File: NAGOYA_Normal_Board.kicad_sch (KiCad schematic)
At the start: 74 parts, among them CN1 value, CN10 value, CN11 value, CN12 value, CN13 value, CN14 RefereeSystem, CN2 value, CN3 value, CN4 value, CN5 value, CN6 value, CN7 value, CN8 value, CN9 value, J1 debug, Q2 DDTC114EUA-7-F, U1 Teensy4.1, U2 TCAN1042HVDR, U3 TCAN1042HVDR, U4 TCAN1042HVDR, U6 TLP172AM, U7 BNO055, Y2 32.768 k

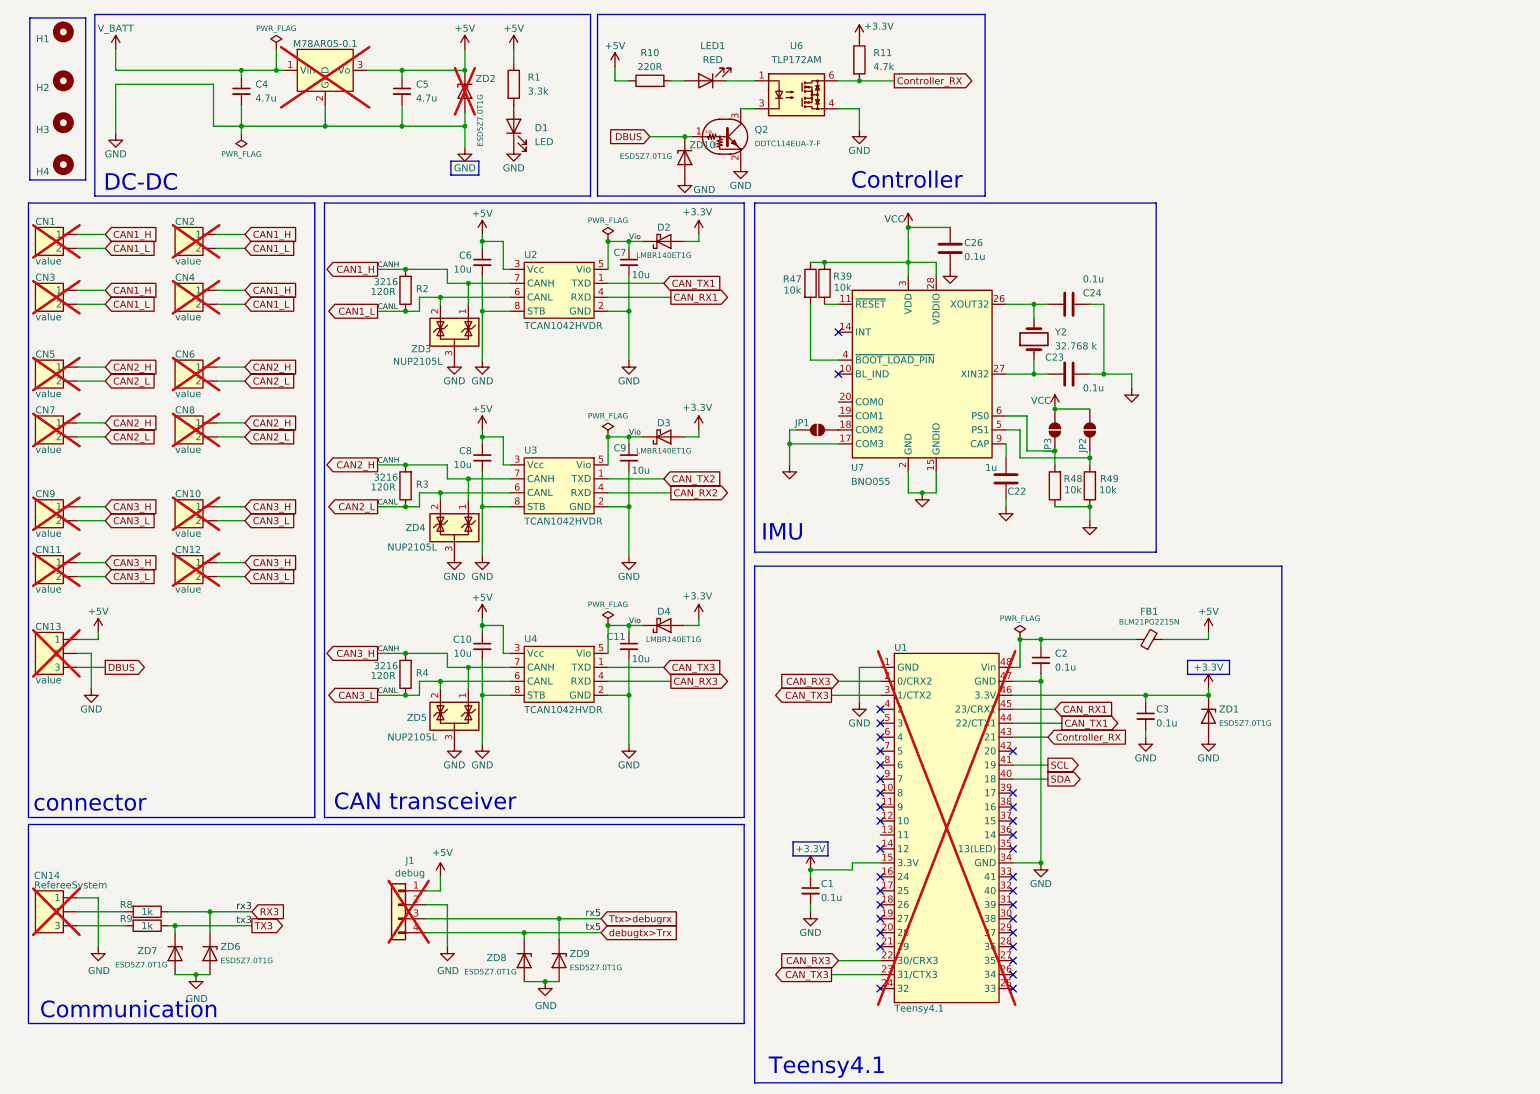
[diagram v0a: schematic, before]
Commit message: RS485を追加
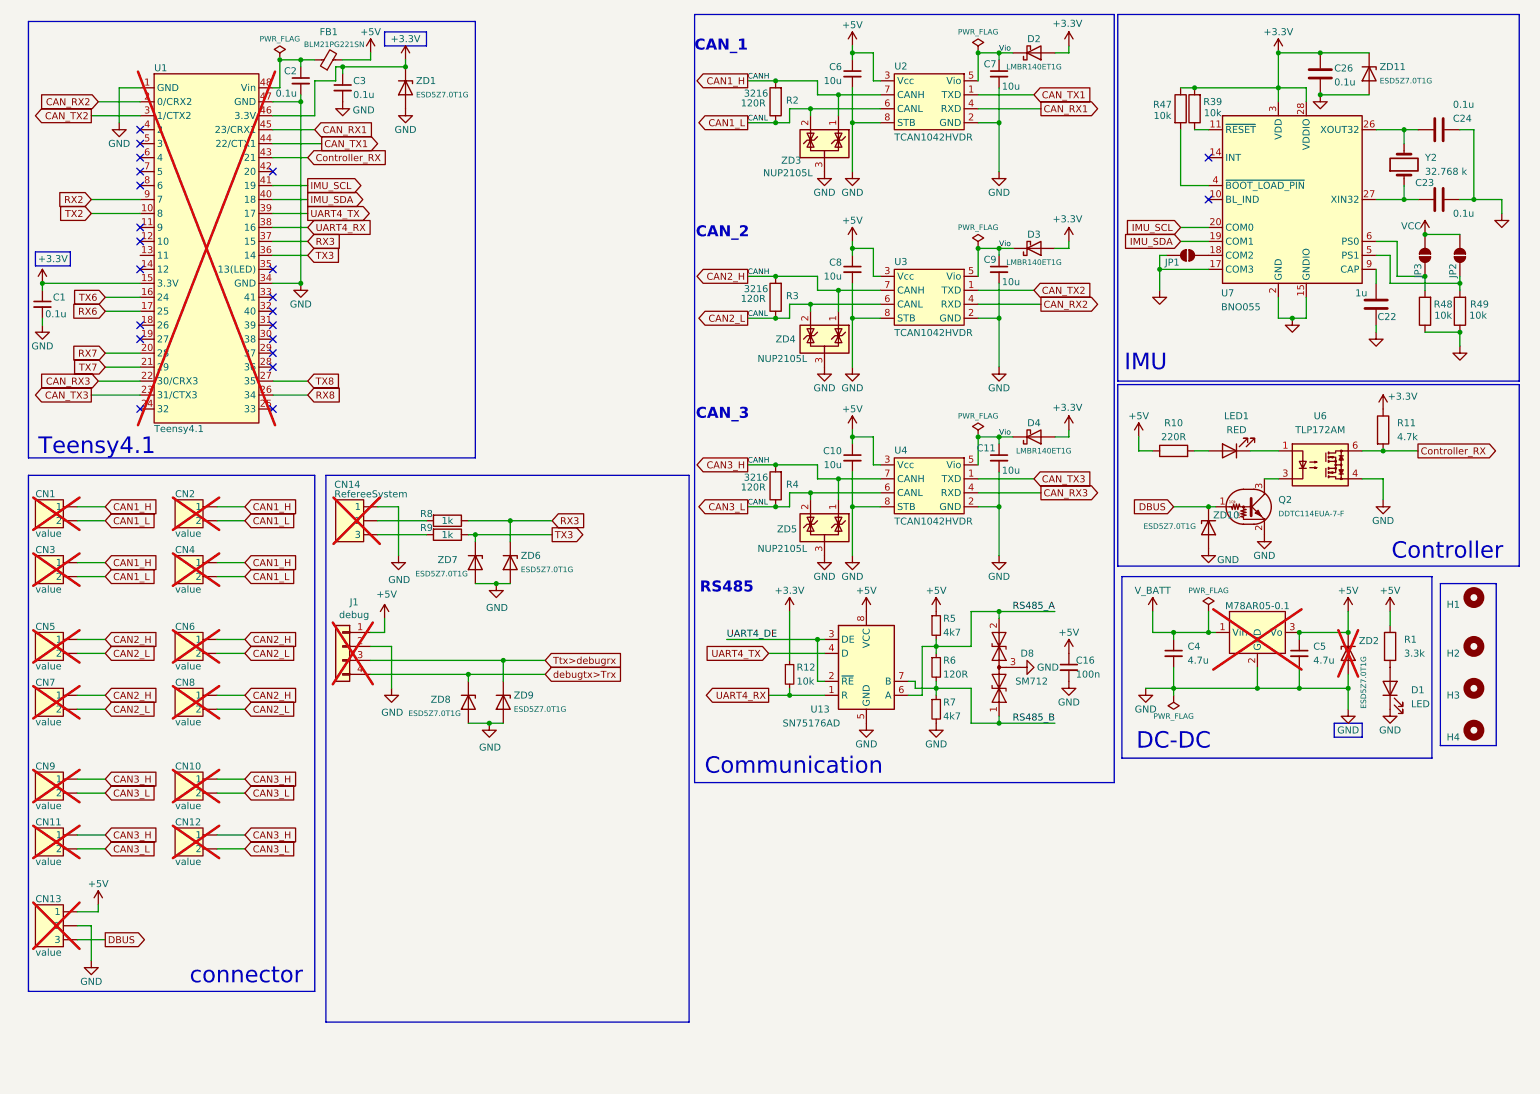
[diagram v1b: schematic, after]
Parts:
- added C16: 100n, Capacitor_SMD:C_0603_1608Metric, symbol Device:C_Small
- added D8: SM712, Package_TO_SOT_SMD:SOT-23, symbol Diode:SM712_SOT23
- added R12: 10k, Resistor_SMD:R_0603_1608Metric, symbol Device:R_Small
- added R5, R7: 4k7, Resistor_SMD:R_0603_1608Metric, symbol Device:R_Small
- added R6: 120R, Resistor_SMD:R_0603_1608Metric, symbol Device:R_Small
- added U13: SN75176AD, Package_SO:SOIC-8_3.9x4.9mm_P1.27mm, symbol Interface_UART:SN75176AD
- added ZD11: ESD5Z7.0T1G, Diode_SMD:D_SOD-523, symbol Diode:ESD5Zxx
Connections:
- net SCL is gone; now on net IMU_SCL: U1.41 (19)
- net SDA is gone; now on net IMU_SDA: U1.40 (18)
- net +3.3V: now also C26.1, R39.2, R47.1, U7.28 (VDDIO), U7.3 (VDD), R12.1, ZD11.1 (K)
- net +5V: now also C16.1, R5.1, U13.8 (VCC)
- net CAN_RX2: now also U1.2 (0/CRX2)
- net CAN_RX3: no longer U1.2 (0/CRX2)
- net CAN_TX2: now also U1.3 (1/CTX2)
- net CAN_TX3: no longer U1.3 (1/CTX2)
- net GND: now also C16.2, D8.3 (common), R7.2, U13.5 (GND)
- net GNDA: now also ZD11.2 (A)
- net RX3: now also U1.37 (15)
- net TX3: now also U1.36 (14)
- net VCC: no longer C26.1, R39.2, R47.1, U7.28 (VDDIO), U7.3 (VDD)
- net TX2: now reaches U1.10 (8)
- net TX6: now reaches U1.16 (24)
- net RX6: now reaches U1.17 (25)
- net RX7: now reaches U1.20 (28)
- net TX7: now reaches U1.21 (29)
- net RX8: now reaches U1.26 (34)
- net TX8: now reaches U1.27 (35)
- net UART4_RX: now reaches U1.38 (16)
- net UART4_RX: now also R12.2, U13.1 (R)
- net UART4_TX: now reaches U1.39 (17)
- net UART4_TX: now also U13.4 (D)
- net RX2: now reaches U1.9 (7)
- net IMU_SDA: now reaches U7.19 (COM1)
- net IMU_SCL: now reaches U7.20 (COM0)
- new net RS485_A: D8.2 (A2), R5.2, R6.1, U13.6 (A)
- new net RS485_B: D8.1 (A1), R6.2, R7.1, U13.7 (B)
- new net UART4_DE: U13.2 (~{RE}), U13.3 (DE)
- no-connect marks 34 -> 22
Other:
- note added: "CAN_1"
- note added: "CAN_2"
- note added: "CAN_3"
- note added: "RS485"
- note removed: "CAN transceiver"
- moved on the sheet: C1, C10, C11, C2, C22, C23, C24, C26, C3, C4, C5, C6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

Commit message: DCDCを変更
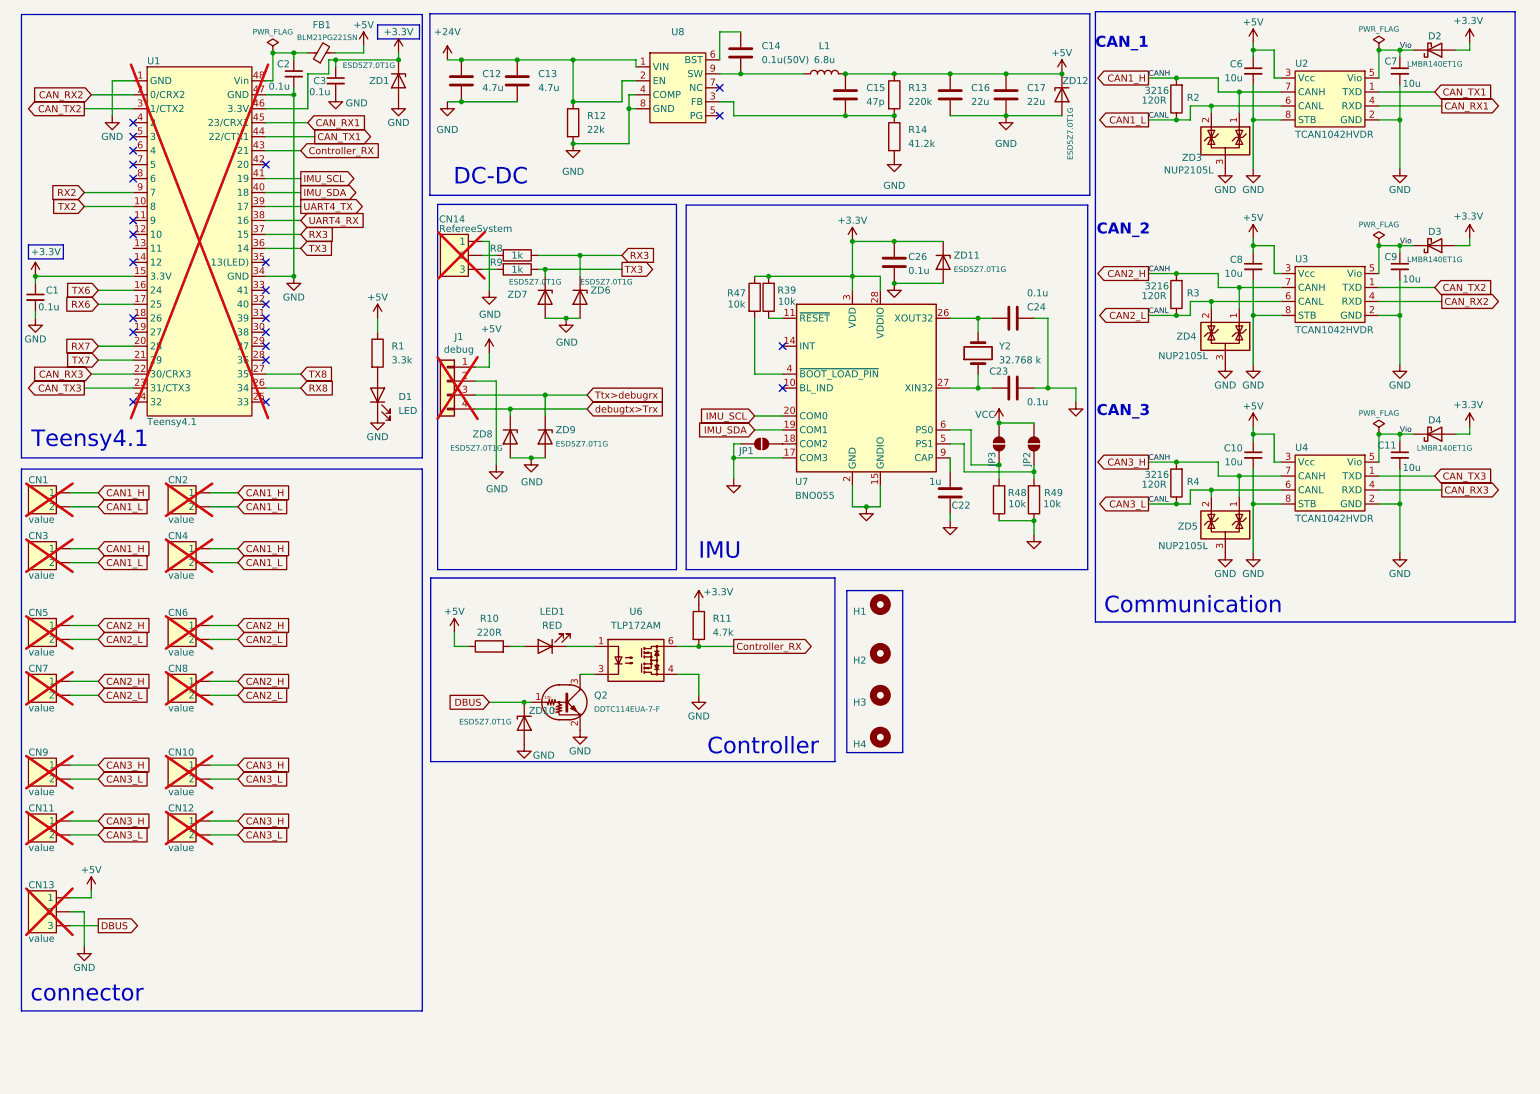
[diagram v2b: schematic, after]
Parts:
- removed C16: 100n, Capacitor_SMD:C_0603_1608Metric, symbol Device:C_Small
- removed C4, C5: 4.7u, Capacitor_SMD:C_1206_3216Metric, symbol Device:C_Small
- removed D8: SM712, Package_TO_SOT_SMD:SOT-23, symbol Diode:SM712_SOT23
- removed M78AR05-0.1: ~, 0_PCB:SIP3_LMS78-12_GAP, symbol 0_circuit:LMS78_2.0R
- removed R12: 10k, Resistor_SMD:R_0603_1608Metric, symbol Device:R_Small
- removed R5, R7: 4k7, Resistor_SMD:R_0603_1608Metric, symbol Device:R_Small
- removed R6: 120R, Resistor_SMD:R_0603_1608Metric, symbol Device:R_Small
- removed U13: SN75176AD, Package_SO:SOIC-8_3.9x4.9mm_P1.27mm, symbol Interface_UART:SN75176AD
- removed ZD2: ESD5Z7.0T1G, Diode_SMD:D_SOD-523, symbol Diode:ESD5Zxx
- added C12, C13: 4.7u, Capacitor_SMD:C_1206_3216Metric, symbol Device:C
- added C14: 0.1u(50V), Capacitor_SMD:C_0402_1005Metric, symbol Device:C
- added C15: 47p, Capacitor_SMD:C_0402_1005Metric, symbol Device:C
- added C16, C17: 22u, Resistor_SMD:R_1206_3216Metric, symbol Device:C
- added L1: 6.8u, Inductor_SMD:L_TracoPower_TCK-047_5.2x5.8mm, symbol Device:L
- added R12: 22k, Resistor_SMD:R_0805_2012Metric, symbol Device:R
- added R13: 220k, Resistor_SMD:R_0201_0603Metric, symbol Device:R
- added R14: 41.2k, Resistor_SMD:R_0201_0603Metric, symbol Device:R
- added U8: ~, TanekonModule:V-DFN3020-13-A_L3.0-W2.0-P0.45-BL-EP_AP6335X, symbol TanekonModule:AP63357DV-7
- added ZD12: ESD5Z7.0T1G, Diode_SMD:D_SOD-523, symbol Diode:ESD5Zxx
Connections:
- net +5V: now also C15.1, C16.1, C17.1, L1.2, R13.1, ZD12.1 (K)
- net GND: now also C12.2, C13.2, C16.2, C17.2, R12.2, R14.2, U8.4 (COMP), U8.8 (GND), ZD12.2 (A)
- new net: C14.1, U8.6 (BST)
- new net: C14.2, L1.1, U8.9 (SW)
- new net: C15.2, R13.2, R14.1, U8.3 (FB)
- new net +24V: C12.1, C13.1, R12.1, U8.1 (VIN), U8.2 (EN)
- no-connect marks 22 -> 24
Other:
- note removed: "RS485"
- moved on the sheet: C1, C10, C11, C2, C22, C23, C24, C26, C3, C6, C7, C8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

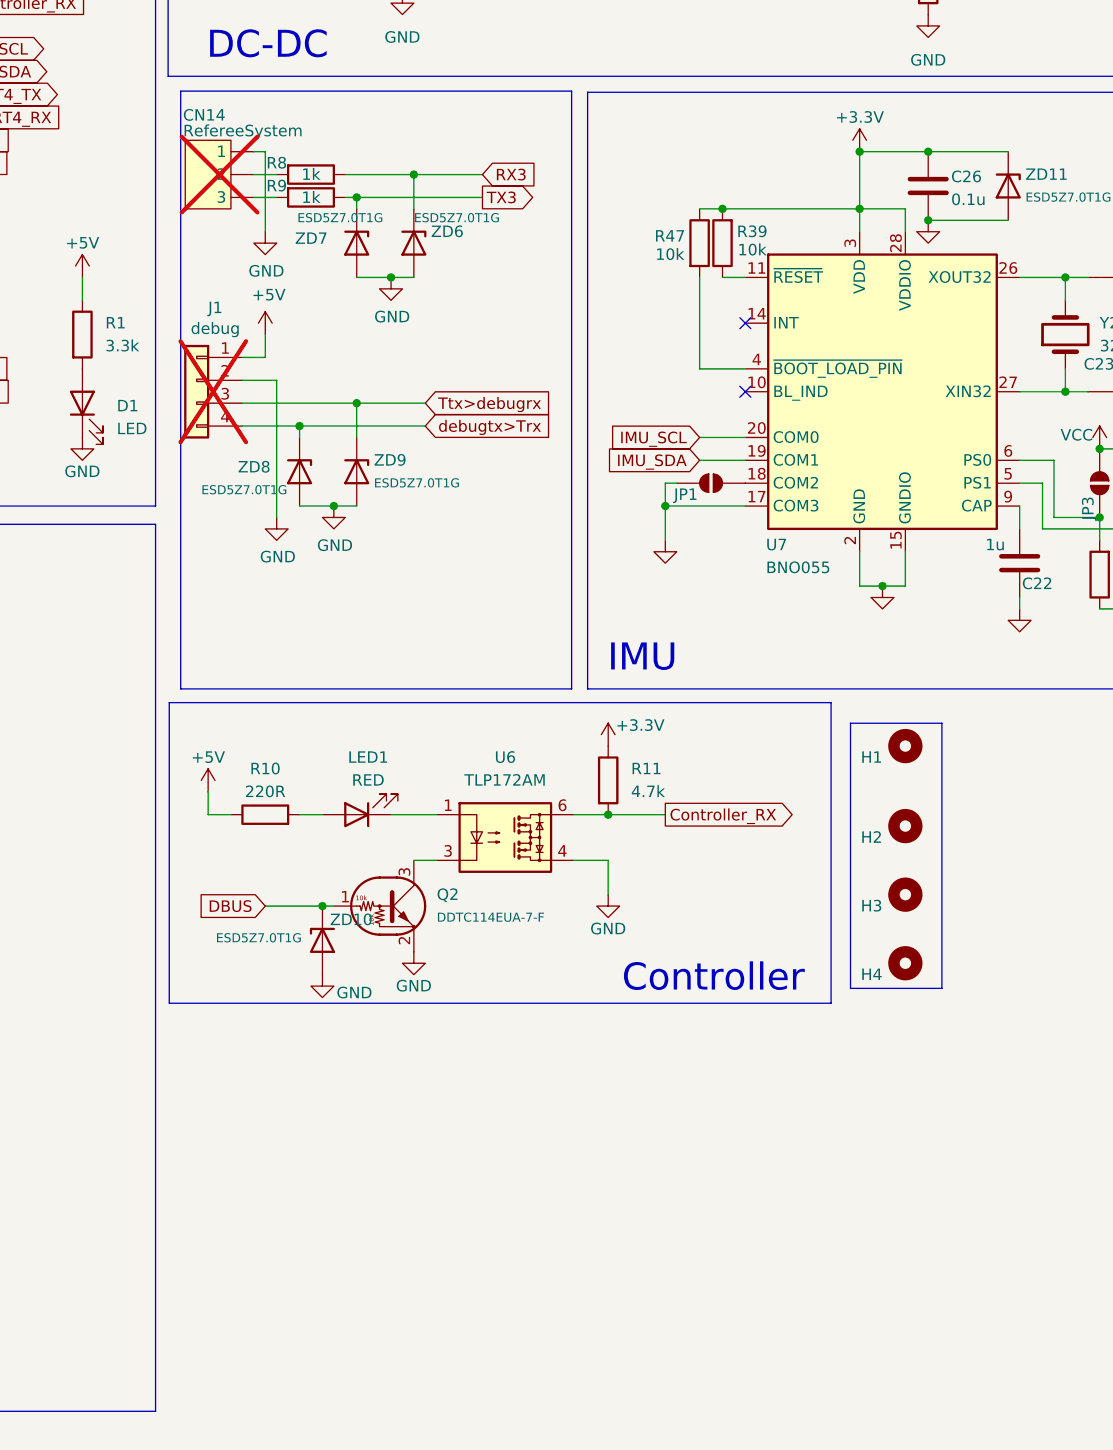
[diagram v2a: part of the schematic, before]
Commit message: USBシリアル変換を追加
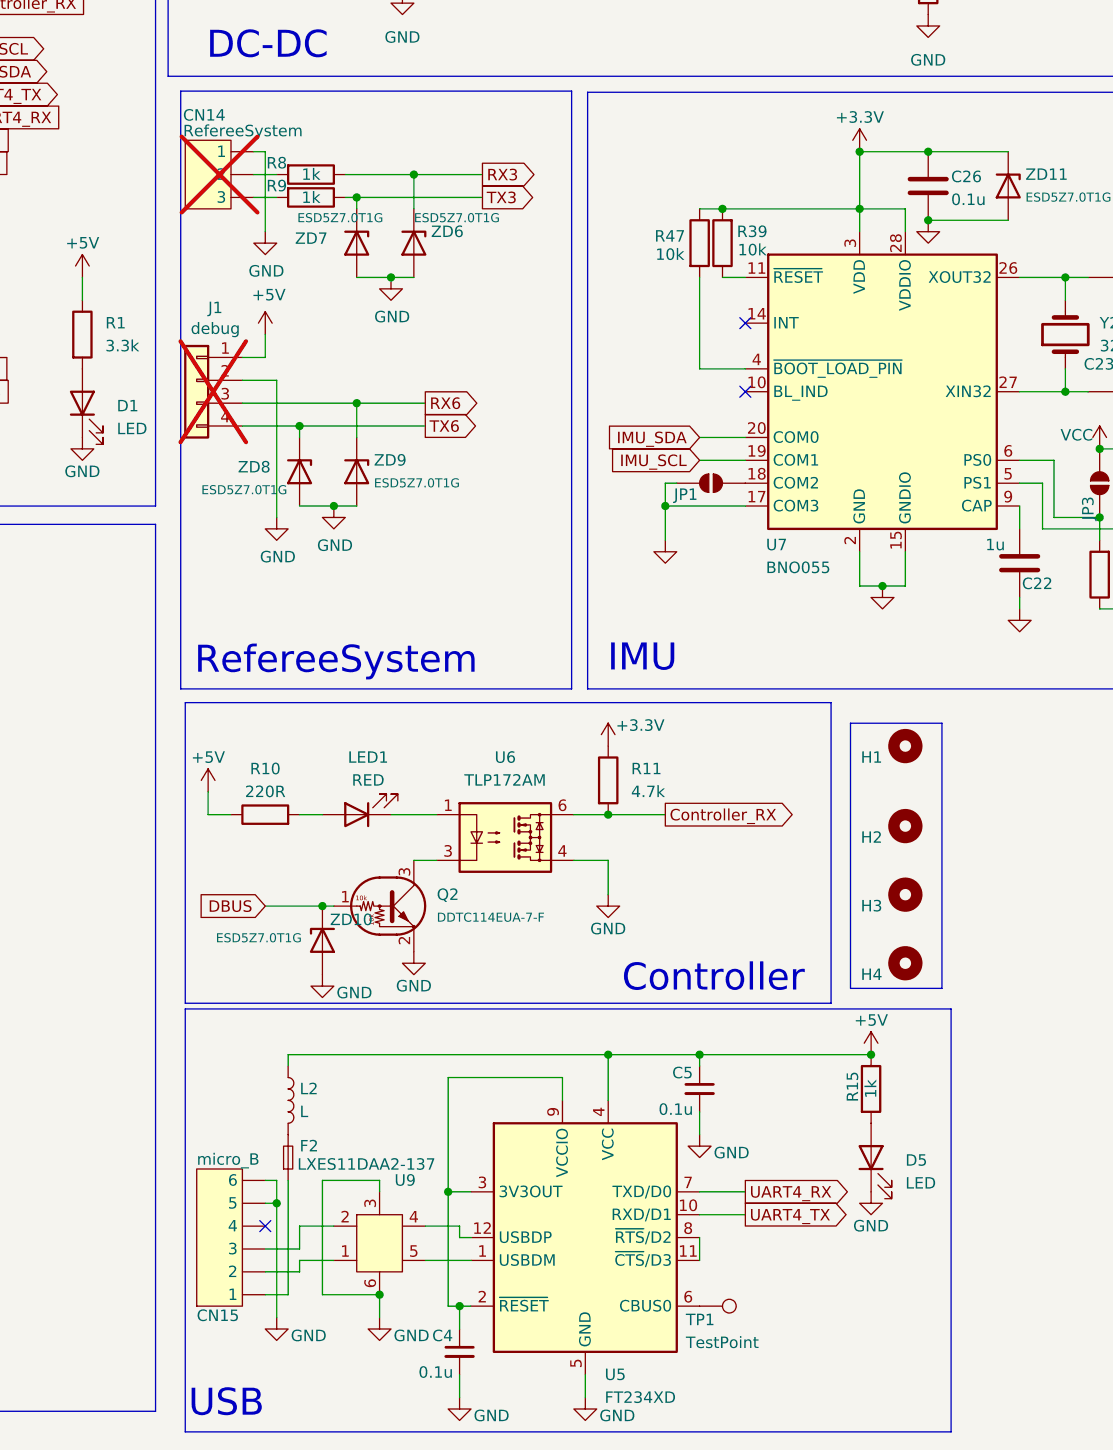
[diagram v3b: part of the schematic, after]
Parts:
- added C4, C5: 0.1u, Capacitor_SMD:C_0603_1608Metric, symbol Device:C_Small
- added CN15: micro_B, symbol 0_circuit:CON_6P
- added D5: LED, LED_SMD:LED_0603_1608Metric, symbol Device:LED
- added F2: Fuse_Small, symbol Device:Fuse_Small
- added L2: L, symbol Device:L
- added R15: 1k, Resistor_SMD:R_0603_1608Metric, symbol Device:R
- added TP1: TestPoint, TestPoint:TestPoint_Pad_1.0x1.0mm, symbol Connector:TestPoint
- added U5: FT234XD, Package_DFN_QFN:WDFN-12-1EP_3x3mm_P0.45mm_EP1.7x2.5mm, symbol Interface_USB:FT234XD
- added U9: LXES11DAA2-137, symbol 0_circuit:LXES11DAA2-137
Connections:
- net Ttx>debugrx is gone; now on net RX6: J1.3 (Pin_3), ZD9.1 (K)
- net debugtx>Trx is gone; now on net TX6: J1.4 (Pin_4), ZD8.1 (K)
- net +5V: now also C5.1, L2.1, R15.1, U5.4 (VCC)
- net GND: now also C4.2, C5.2, CN15.5, CN15.6, D5.1 (K), U5.13 (GND), U5.5 (GND), U9.3, U9.6
- net IMU_SCL: now also U7.19 (COM1); no longer U7.20 (COM0)
- net IMU_SDA: now also U7.20 (COM0); no longer U7.19 (COM1)
- net UART4_RX: now also U5.7 (TXD/D0)
- net UART4_TX: now also U5.10 (RXD/D1)
- new net: CN15.1, F2.1
- new net: F2.2, L2.2
- new net: U5.1 (USBDM), U9.5
- new net: U5.11 (~{CTS}/D3), U5.8 (~{RTS}/D2)
- new net: U5.12 (USBDP), U9.4
- new net: C4.1, U5.2 (~{RESET}), U5.3 (3V3OUT), U5.9 (VCCIO)
- new net: TP1.1, U5.6 (CBUS0)
- new net: CN15.2, U9.1
- new net: CN15.3, U9.2
- new net: D5.2 (A), R15.2
- no-connect marks 24 -> 25
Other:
- note added: "RefereeSystem"
- note added: "USB"
